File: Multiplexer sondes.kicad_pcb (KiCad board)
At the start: 4 copper layers, 68.6 x 53.3 mm, 33 parts, among them J1 Conn_Coaxial, J2 DB9_Female_MountingHoles, K0 REED_1C, K1 REED_1C, K10 Reed_1A, K11 REED_1C, K111 REED_1C, K112 REED_1C, K12 REED_1C, K121 REED_1C, K122 REED_1C, K2 REED_1C, K20 Reed_1A, K21 REED_1C, K211 REED_1C, K212 REED_1C, K22 REED_1C, K221 REED_1C, K222 REED_1C, K30 Reed_1A, K40 Reed_1A

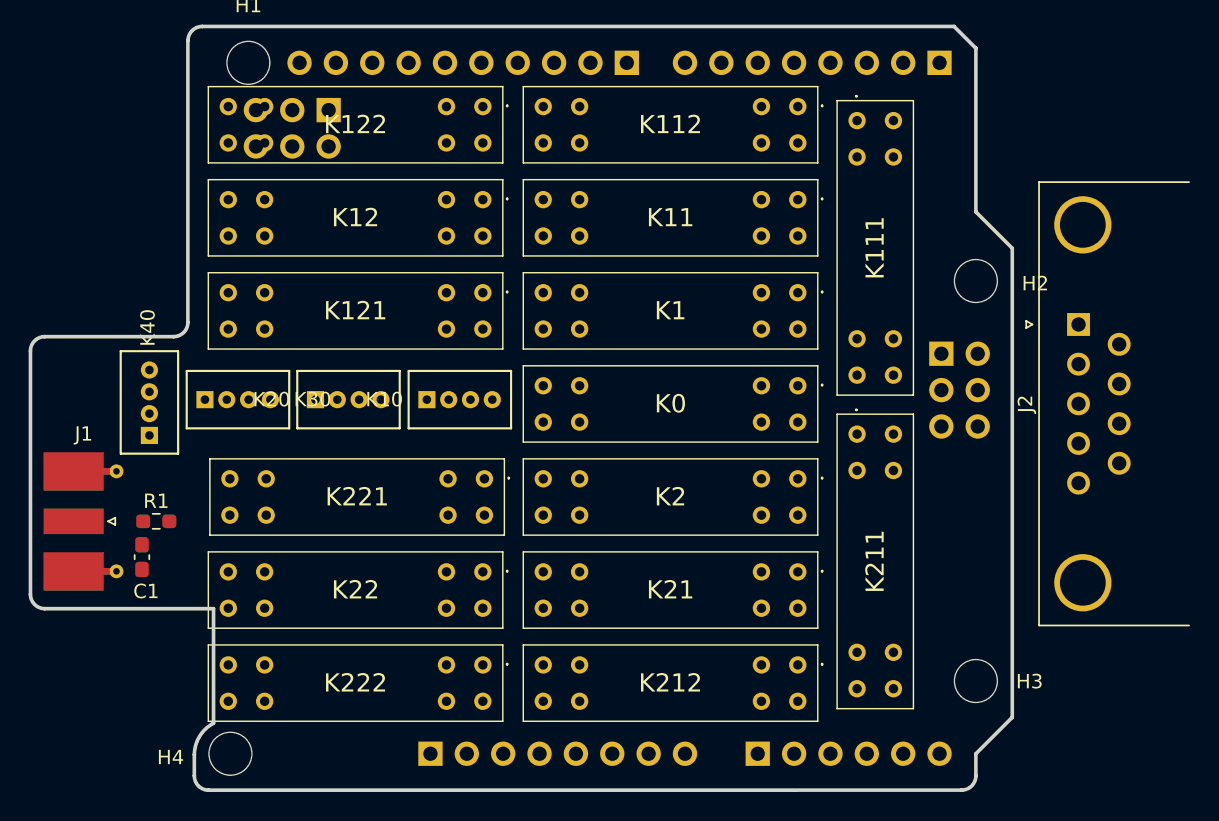
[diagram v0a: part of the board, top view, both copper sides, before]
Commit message: deleted part of the arduino's pins began routing
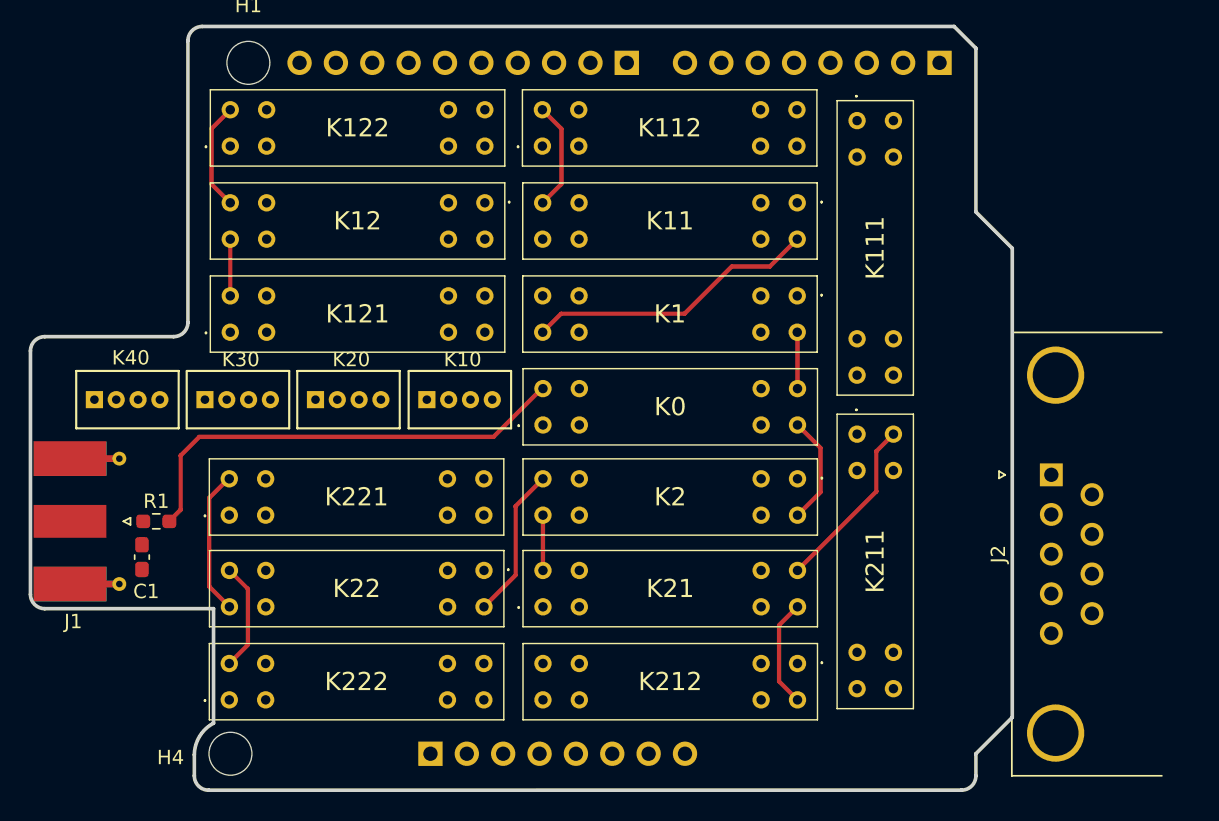
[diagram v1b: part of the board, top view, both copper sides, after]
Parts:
- removed AD1: Conn_01x06_Female, Connector_PinHeader_2.54mm:PinHeader_1x06_P2.54mm_Vertical
- removed H2, H3: MountingHole, MountingHole:MountingHole_3mm
- removed ICSP1, ICSP2: Conn_02x03_Odd_Even, Connector_PinSocket_2.54mm:PinSocket_2x03_P2.54mm_Vertical
- J1: footprint Connector_Coaxial:SMA_Molex_73251-2120_EdgeMount_Horizontal -> Connector_Coaxial:SMA_Molex_73251-1153_EdgeMount_Horizontal
- K10, K20, K30, K40: footprint LibPersoNadj:Relay_reed_comus_3570 -> LibPersoNadj:Relay_reed_comus_3570-1517
- moved K112 18.1 mm to (150.0, 86.7), turned to 0 degrees
- moved K0 18.0 mm to (150.0, 106.2), turned to 0 degrees
- moved K221 18.0 mm to (128.1, 112.5), turned to 0 degrees
- moved K21 18.0 mm to (150.0, 118.9), turned to 0 degrees
- moved K222 17.9 mm to (128.1, 125.4), turned to 0 degrees
- moved K121 17.9 mm to (128.2, 99.7), turned to 0 degrees
- moved K122 17.9 mm to (128.2, 86.7), turned to 0 degrees
- moved J2 10.7 mm to (185.5, 109.7)
- moved K40 4.58 mm to (118.7, 104.4), turned to 0 degrees
- moved J1 1.47 mm to (118.7, 112.9), turned to 0 degrees
- moved K12 0.26 mm to (145.9, 90.7)
- moved K1 0.22 mm to (167.8, 97.2)
- moved K11 0.22 mm to (167.8, 90.7)
- moved K22 0.13 mm to (145.9, 116.3)
- moved K212 0.10 mm to (167.8, 122.8)
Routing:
- net /1to16_reedRelay/1to4_reedRelay5/S1234: track 0.00 -> 32.3 mm
- net /1to16_reedRelay/S1-4: track 0.00 -> 20.5 mm
- net /1to16_reedRelay/1to4_reedRelay7/S12: track 0.00 -> 12.3 mm
- net /1to16_reedRelay/S13-16: track 0.00 -> 10.6 mm
- net /1to16_reedRelay/1to4_reedRelay6/S12: track 0.00 -> 10.2 mm
- net /1to16_reedRelay/1to4_reedRelay5/S34: track 0.00 -> 7.63 mm
- net /1to16_reedRelay/1to4_reedRelay4/S34: track 0.00 -> 7.59 mm
- net /1to16_reedRelay/1to4_reedRelay3/S34: track 0.00 -> 7.59 mm
- net /1to16_reedRelay/1to4_reedRelay6/S34: track 0.00 -> 7.57 mm
- net /1to16_reedRelay/1to4_reedRelay7/S34: track 0.00 -> 7.57 mm
- net /1to16_reedRelay/1to4_reedRelay5/S12: track 0.00 -> 4.05 mm
- net /1to16_reedRelay/1to4_reedRelay3/S12: track 0.00 -> 3.96 mm
- net /1to16_reedRelay/S9-12: track 0.00 -> 3.96 mm

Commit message: v0.0 routed
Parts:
- moved K20 31.8 mm to (165.9, 104.9)
- moved K30 31.8 mm to (158.2, 104.9)
- moved K12 24.0 mm to (169.9, 90.8)
- moved K121 24.0 mm to (152.2, 99.9)
- moved K122 24.0 mm to (152.2, 86.9)
- moved K22 24.0 mm to (169.9, 116.5)
- moved K221 24.0 mm to (152.1, 112.7)
- moved K222 24.0 mm to (152.1, 125.6)
- moved K0 20.9 mm to (129.1, 106.4)
- moved K1 20.9 mm to (146.9, 97.4)
- moved K11 20.9 mm to (146.9, 90.9)
- moved K112 20.9 mm to (129.1, 86.9)
- moved K2 20.9 mm to (146.9, 110.1)
- moved K21 20.9 mm to (129.1, 119.1)
- moved K212 20.9 mm to (146.9, 123.0)
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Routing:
- net /C4: track 0.00 -> 152.3 mm
- net /C3: track 0.00 -> 134.7 mm
- net /S4: track 0.00 -> 88.7 mm
- net /S3: track 0.00 -> 60.2 mm
- net /1to16_reedRelay/1to4_reedRelay4/S12: track 0.00 -> 52.9 mm
- net /S8: track 0.00 -> 52.0 mm
- net /1to16_reedRelay/S5-8: track 0.00 -> 50.9 mm
- net /1to16_reedRelay/S13-16: track 10.6 -> 51.5 mm
- net /C2: track 0.00 -> 38.6 mm
- net /S7: track 0.00 -> 38.2 mm
- net /S5: track 0.00 -> 37.0 mm
- net /S6: track 0.00 -> 35.2 mm
- net /C1: track 0.00 -> 28.0 mm
- net /1to16_reedRelay/1to4_reedRelay7/S12: track 12.3 -> 36.0 mm
- net /1to16_reedRelay/1to4_reedRelay5/S1234: track 32.3 -> 11.1 mm
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- added copper zone on In2.Cu, net /+5V_Ard_1
- added copper zone on B.Cu, net GND
- added copper zone on F.Cu, net GND
- added copper zone on In1.Cu, net GND
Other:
- board size 68.6 x 53.3 mm -> 78.8 x 53.3 mm

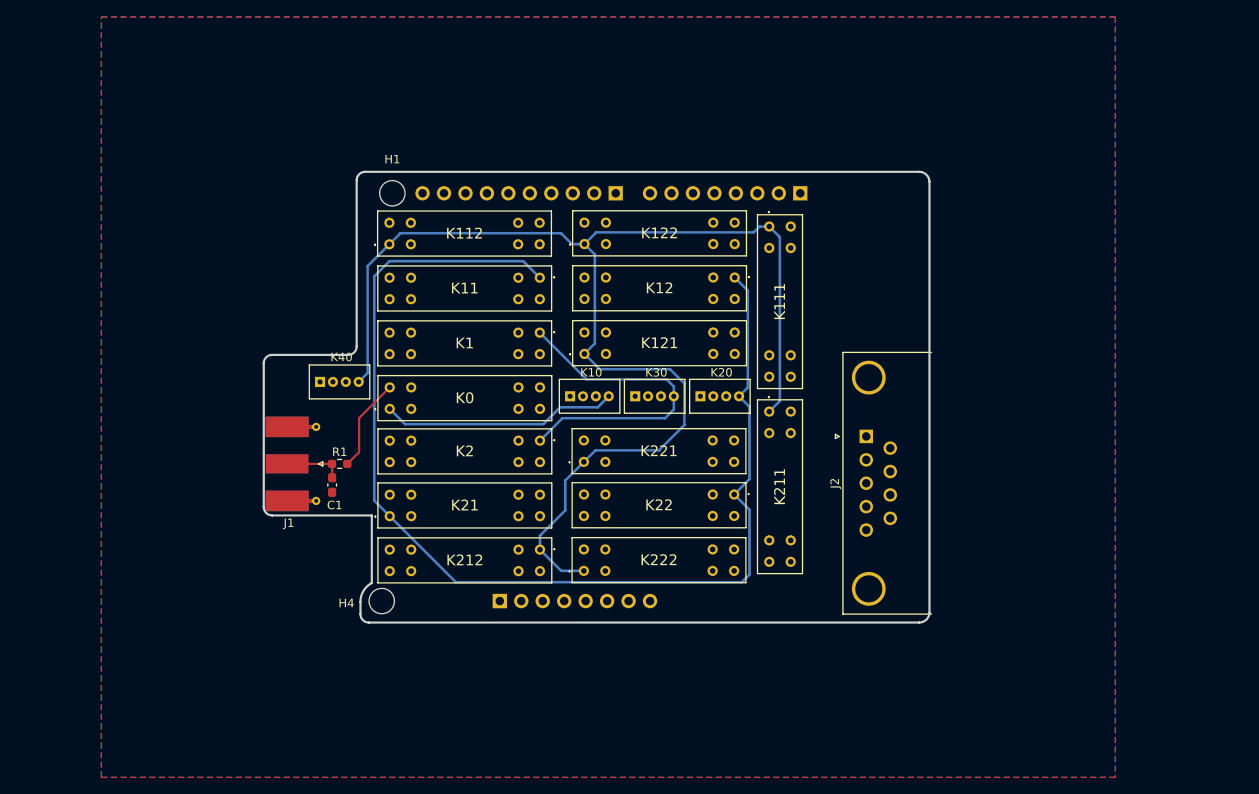
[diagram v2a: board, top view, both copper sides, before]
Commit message: Passed to 1 relay per signal with Arduino Mega
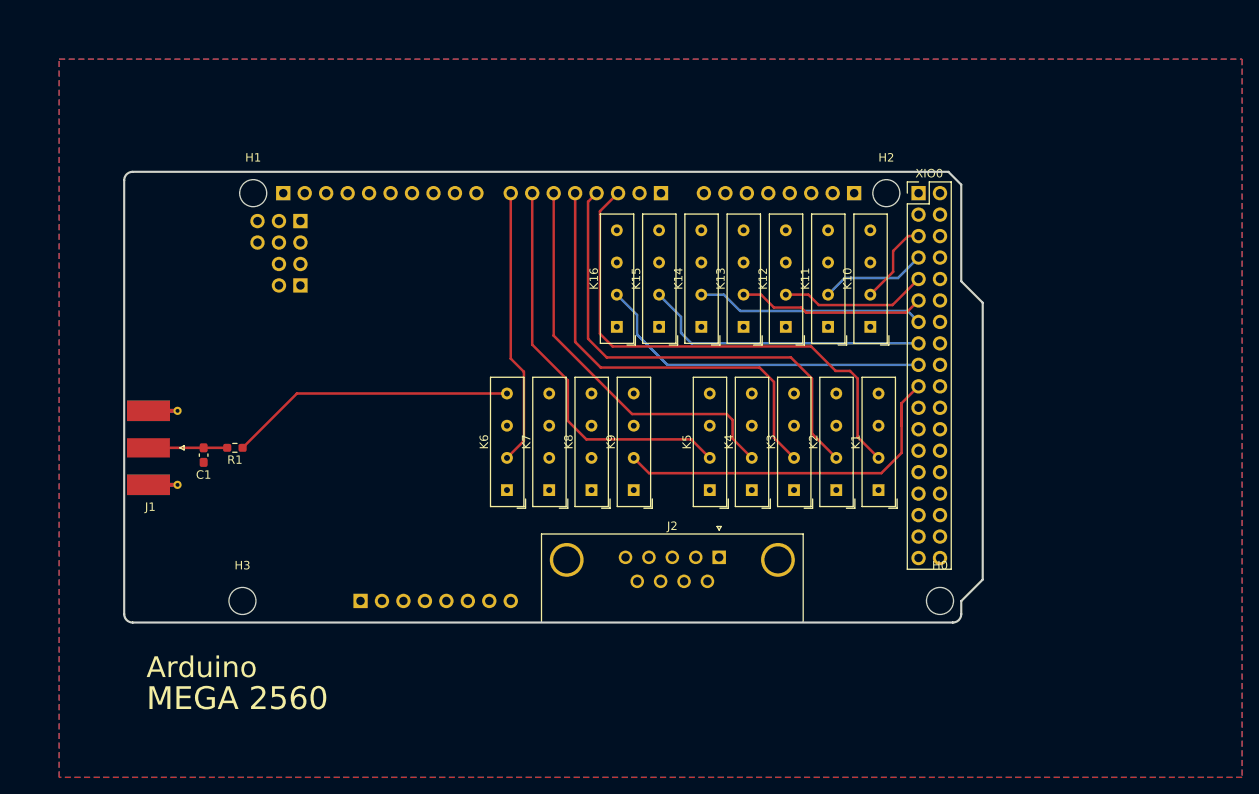
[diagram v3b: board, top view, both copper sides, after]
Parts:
- removed H4: MountingHole, MountingHole:MountingHole_3mm
- removed IOH1: Conn_01x10_Female, Connector_PinHeader_2.54mm:PinHeader_1x10_P2.54mm_Vertical
- removed IOL1, POWER1: Conn_01x08_Female, Connector_PinHeader_2.54mm:PinHeader_1x08_P2.54mm_Vertical
- removed K0, K111, K112, K121, K122, K21, K211, K212, K22, K221, K222: REED_1C, LibPersoNadj:Relay_reed_1C
- removed K20, K30, K40: Reed_1A, LibPersoNadj:Relay_reed_comus_3570-1517
- added COMMUNICATION0: FH254-108DF08500V, Connector_PinHeader_2.54mm:PinHeader_1x08_P2.54mm_Vertical, B.Cu at (184.1, 80.9)
- added H0: MountingHole_Pad, MountingHole:MountingHole_3.2mm_M3, F.Cu at (194.2, 129.1)
- added H2: MountingHole_Pad, MountingHole:MountingHole_3.2mm_M3, F.Cu at (187.9, 80.9)
- added H3: MountingHole_Pad, MountingHole:MountingHole_3.2mm_M3, F.Cu at (111.7, 129.1)
- added ICSP1: ICSP, Connector_PinSocket_2.54mm:PinSocket_2x03_P2.54mm_Vertical, B.Cu at (118.6, 84.2)
- added JP5: 2x2M - NM, Connector_PinSocket_2.54mm:PinSocket_2x02_P2.54mm_Vertical, B.Cu at (118.6, 91.8)
- added JP6: FH254-110DF08500V, Connector_PinHeader_2.54mm:PinHeader_1x10_P2.54mm_Vertical, B.Cu at (116.5, 80.9)
- added K13: 3570-1411-053, Relay_THT:Relay_SPST_StandexMeder_MS_Form1AB, F.Cu at (171.0, 96.7)
- added K14: 3570-1411-053, Relay_THT:Relay_SPST_StandexMeder_MS_Form1AB, F.Cu at (166.0, 96.7)
- added K15: 3570-1411-053, Relay_THT:Relay_SPST_StandexMeder_MS_Form1AB, F.Cu at (161.0, 96.7)
- added K16: 3570-1411-053, Relay_THT:Relay_SPST_StandexMeder_MS_Form1AB, F.Cu at (156.0, 96.7)
- added K3: 3570-1411-053, Relay_THT:Relay_SPST_StandexMeder_MS_Form1AB, F.Cu at (177.0, 116.0)
- added K4: 3570-1411-053, Relay_THT:Relay_SPST_StandexMeder_MS_Form1AB, F.Cu at (172.0, 116.0)
- added K5: 3570-1411-053, Relay_THT:Relay_SPST_StandexMeder_MS_Form1AB, F.Cu at (167.0, 116.0)
- added K6: 3570-1411-053, Relay_THT:Relay_SPST_StandexMeder_MS_Form1AB, F.Cu at (143.0, 116.0)
- added K7: 3570-1411-053, Relay_THT:Relay_SPST_StandexMeder_MS_Form1AB, F.Cu at (148.0, 116.0)
- added K8: 3570-1411-053, Relay_THT:Relay_SPST_StandexMeder_MS_Form1AB, F.Cu at (153.0, 116.0)
- added K9: 3570-1411-053, Relay_THT:Relay_SPST_StandexMeder_MS_Form1AB, F.Cu at (158.0, 116.0)
- added POWER0: FH254-108DF08500V, Connector_PinHeader_2.54mm:PinHeader_1x08_P2.54mm_Vertical, B.Cu at (125.7, 129.1)
- added PWML0: FH254-108DF08500V, Connector_PinHeader_2.54mm:PinHeader_1x08_P2.54mm_Vertical, B.Cu at (161.2, 80.9)
- added XIO0: 18x2F-H8.5, Connector_PinHeader_2.54mm:PinHeader_2x18_P2.54mm_Vertical, F.Cu at (191.7, 80.9)
- H1: value MountingHole -> MountingHole_Pad; footprint MountingHole:MountingHole_3mm -> MountingHole:MountingHole_3.2mm_M3
- J1: value Conn_Coaxial -> OIP
- K1, K11, K12, K2: value REED_1C -> 3570-1411-053; footprint LibPersoNadj:Relay_reed_1C -> Relay_THT:Relay_SPST_StandexMeder_MS_Form1AB
- K10: value Reed_1A -> 3570-1411-053; footprint LibPersoNadj:Relay_reed_comus_3570-1517 -> Relay_THT:Relay_SPST_StandexMeder_MS_Form1AB
- moved K1 44.2 mm to (187.0, 116.0), turned to 90 degrees
- moved K10 36.5 mm to (186.0, 96.7), turned to 90 degrees
- moved K2 35.6 mm to (182.0, 116.0), turned to 90 degrees
- moved K11 34.6 mm to (181.0, 96.7), turned to 90 degrees
- moved J2 22.5 mm to (168.1, 124.0), turned to 0 degrees
- moved J1 16.5 mm to (102.3, 111.0)
- moved H1 16.5 mm to (113.0, 80.9)
- moved C1 15.6 mm to (107.1, 111.9)
- moved R1 12.5 mm to (110.8, 111.0)
- moved K12 8.41 mm to (176.0, 96.7), turned to 90 degrees
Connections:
- net Net-(C1-Pad1) renamed /OutF
- K1 pad 1: /C2 -> /S1
- K1 pad 3: GND -> /D2
- K1 pad 5: /1to16_reedRelay/S1-4 -> GND
- K1 pad 7: unconnected-(K1-Pad7) -> /Out
- K10 pad 1: unconnected-(K10-Pad1) -> /S10
- K10 pad 3: /+5V_Ard_1 -> /D24
- K11 pad 1: /C3 -> /S11
- K11 pad 3: GND -> /D26
- K11 pad 5: /1to16_reedRelay/1to4_reedRelay4/S12 -> GND
- K11 pad 7: unconnected-(K11-Pad7) -> /Out
- K12 pad 1: /C3 -> /S12
- K12 pad 3: GND -> /D28
- K12 pad 5: /1to16_reedRelay/1to4_reedRelay3/S12 -> GND
- K12 pad 7: unconnected-(K12-Pad7) -> /Out
- K2 pad 1: /C2 -> /S2
- K2 pad 3: GND -> /D3
- K2 pad 5: /1to16_reedRelay/S9-12 -> GND
- K2 pad 7: unconnected-(K2-Pad7) -> /Out
- R1 pad 1: /1to16_reedRelay/1to4_reedRelay5/S1234 -> /Out
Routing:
- net /C4: track 152.3 -> 0.00 mm
- net /C3: track 134.7 -> 0.00 mm
- net /Out: track 0.00 -> 77.9 mm
- net /S4: track 88.7 -> 16.1 mm
- net /D2: track 0.00 -> 60.6 mm
- net /D3: track 0.00 -> 56.7 mm
- net /D4: track 0.00 -> 53.1 mm
- net /1to16_reedRelay/1to4_reedRelay4/S12: track 52.9 -> 0.00 mm
- net /1to16_reedRelay/S13-16: track 51.5 -> 0.00 mm
- net /1to16_reedRelay/S5-8: track 50.9 -> 0.00 mm
- net /D5: track 0.00 -> 47.6 mm
- net /D6: track 0.00 -> 47.3 mm
- net /D38: track 0.00 -> 45.8 mm
- net /S3: track 60.2 -> 18.6 mm
- net /D36: track 0.00 -> 40.5 mm
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- added copper zone on In2.Cu, net GND
- removed copper zone on In2.Cu, net /+5V_Ard_1
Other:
- board size 78.8 x 53.3 mm -> 101.6 x 53.3 mm
- board text added: "Arduino"
- board text added: "MEGA 2560"
- board text removed: "IOL1"

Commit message: Command stepper done
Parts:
- removed JP5: 2x2M - NM, Connector_PinSocket_2.54mm:PinSocket_2x02_P2.54mm_Vertical
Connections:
- net /PB4 renamed /D10
- net /PB5 renamed /D11
- net /PB6 renamed /D12
- net /PB7 renamed /D13
- JP6 pad 10: /PH5 -> /D8
- JP6 pad 9: /PH6 -> /D9
- K10 pad 7: /Out -> /Relais/out10
- K11 pad 7: /Out -> /Relais/out11
- K12 pad 7: /Out -> /Relais/out12
- K13 pad 7: /Out -> /Relais/out13
- K14 pad 7: /Out -> /Relais/out14
- K15 pad 7: /Out -> /Relais/out15
- K16 pad 7: /Out -> /Relais/out16
- K8 pad 5: unconnected-(K8-Pad5) -> GND
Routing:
- net /D9: track 0.00 -> 47.0 mm
- net /D8: track 0.00 -> 34.9 mm
- net +5V: track 0.00 -> 2.54 mm
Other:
- outline, holes or cut-outs redrawn
- board text removed: "Arduino"
- board text removed: "MEGA 2560"
